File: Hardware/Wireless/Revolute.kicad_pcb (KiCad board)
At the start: 4 copper layers, 20 x 20 mm, 54 parts, among them Q1 AO3407, U1 BQ27441-G1, U2 nrf52833_qfn40, U3 AS5600, U4 AP2112K-3.3, U5 BQ24075RGT, U7 MAX16054, X1 32.768 kHz, X2 32MHZ

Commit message: worked on wireless
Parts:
- removed the ? at (171.0, 95.0)
- removed Q1: AO3407, Package_TO_SOT_SMD:SOT-23
- removed R10: 5.1K, Resistor_SMD:R_0402_1005Metric
- removed U7: MAX16054, Package_TO_SOT_SMD:SOT-23-6
- added ?: , , F.Cu at (179.1, 96.5)
- added ?: , , F.Cu at (178.7, 94.7)
- added U6: Button, Library:buttoncompliant, F.Cu at (171.0, 95.0)
- added U8: ~, Library:BK13C06-10DP, B.Cu at (175.0, 94.8)
- AE1: value ANT3216LL00R2400A -> Antenna
- moved C26 4.76 mm to (175.6, 102.8)
- moved C22 4.76 mm to (175.6, 101.8)
- moved U4 1.37 mm to (176.4, 99.1), turned to 90 degrees
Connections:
- C22 pad 1: vSYSTEM -> OUT
- C26 pad 1: vSYSTEM -> OUT
- U2 pad 33: unconnected-(U2-P0.28/AIN4-Pad33) -> Net-(U2-P0.28/AIN4)
- U4 pad 1: vSYSTEM -> OUT
- U4 pad 3: vSYSTEM -> OUT
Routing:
- net D+: track 0.76 -> 19.8 mm, vias 1 -> 2
- net D-: track 0.50 -> 17.6 mm, vias 1 -> 2
- net swd: track 0.74 -> 13.4 mm, vias 1 -> 2
- net swc: track 0.48 -> 13.0 mm, vias 1 -> 2
- net RESET: track 0.80 -> 13.1 mm, vias 1 -> 2
- net Net-(U7-IN): track 9.19 -> 0.00 mm, vias 1 -> 0
- net GND: track 20.3 -> 27.7 mm, vias 10 -> 24
- net vSYSTEM: track 7.14 -> 0.00 mm
- net OUT: track 22.9 -> 17.7 mm
- net Net-(Q1-G): track 4.33 -> 0.00 mm
- net Batteryin: track 6.56 -> 10.3 mm, vias 2 -> 4
- net VDD_nRF: track 18.6 -> 22.3 mm, vias 8 -> 10
- net Net-(U2-P0.28/AIN4): track 0.00 -> 3.53 mm, vias 0 -> 1
- net CLEAR: track 2.53 -> 0.00 mm
- net P0.15: track 28.6 -> 31.0 mm, vias 3 -> 4
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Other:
- board size 20 x 20 mm -> 19.8 x 20 mm
- board text added: "D+"
- board text added: "D-"
- board text added: "GND"
- board text added: "RST"
- board text added: "SWC"
- board text added: "SWD"
- board text added: "VDD"

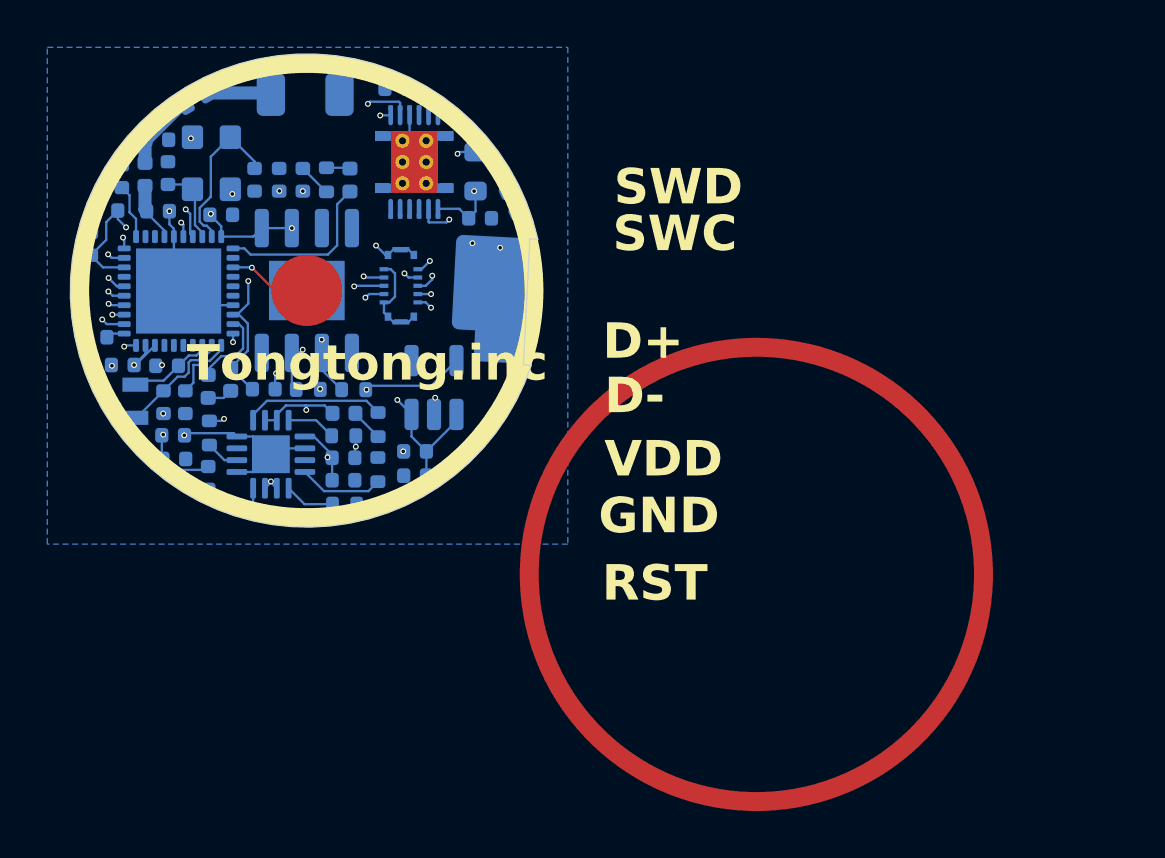
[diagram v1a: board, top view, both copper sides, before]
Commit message: added debug board (work in progress)
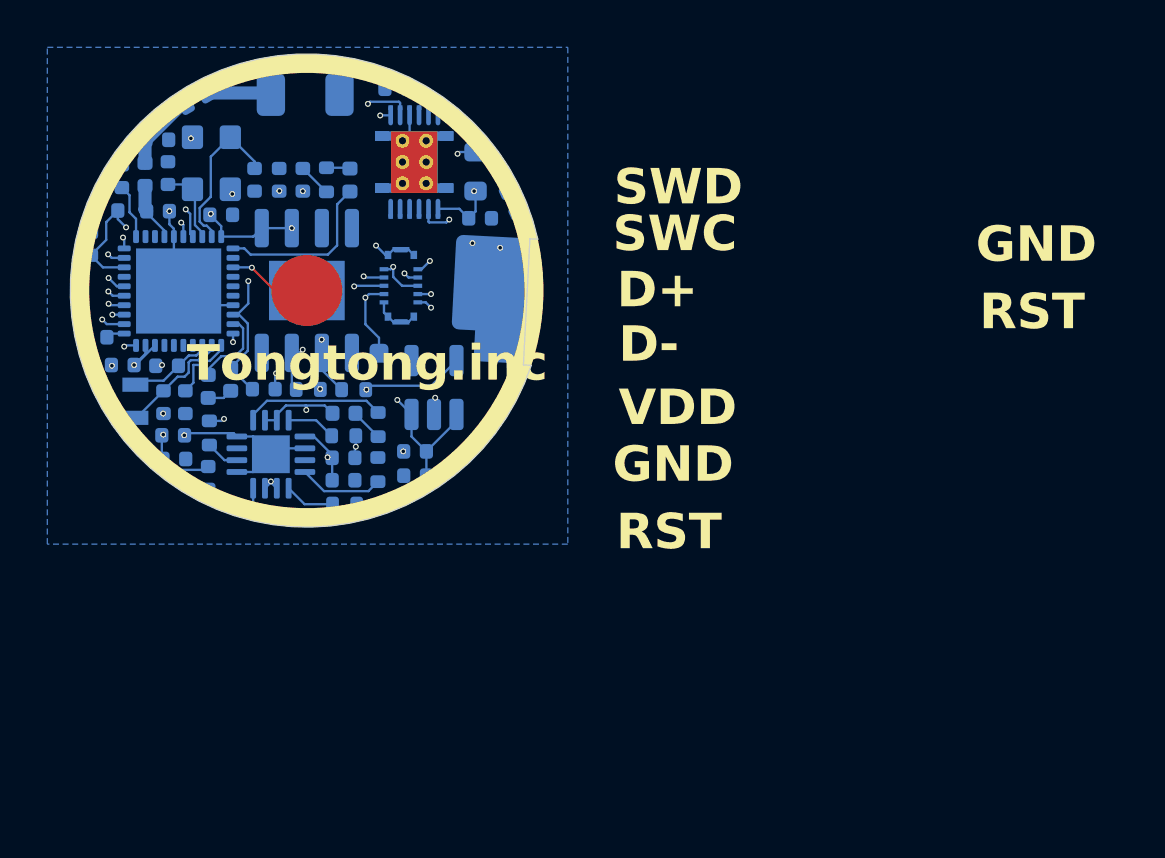
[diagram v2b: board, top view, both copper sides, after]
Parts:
- added ?: , , F.Cu at (174.1, 97.7)
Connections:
- U8 pad 1: GND -> OUT
- U8 pad 8: VDD_nRF -> OUT
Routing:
- net OUT: track 17.7 -> 25.4 mm, vias 3 -> 4
- net RESET: track 13.1 -> 15.7 mm
- net GND: track 27.7 -> 25.6 mm
- net VDD_nRF: track 22.3 -> 21.4 mm, vias 10 -> 9
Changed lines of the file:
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@@
   (net 59 "GPOUT")
   (footprint "" (layer "F.Cu")
+    (at 174.05 97.65)
+    (fp_text reference "" (at 0 0) (layer "F.SilkS")
+        (effects (font (size 1.27 1.27) (thickness 0.15)))
+    )
+    (fp_text value "" (at 0 0) (layer "F.SilkS")
+        (effects (font (size 1.27 1.27) (thickness 0.15)))
+    )
+    (pad "4" smd roundrect (at 0 0 90) (size 0.8 0.8) (layers "B.Cu" "B.Paste" "B.Mask") (roundrect_rratio 0.25)
+      (net 19 "RESET") (pinfunction "NC") (pintype "no_connect"))
+  )
+  (footprint "" (layer "F.Cu")
     (at 179.121196 96.534972 -3)
     (fp_text reference "" (at 0 0 177) (layer "F.SilkS")
@@
       (stroke (width 0.15) (type default)) (fill none) (layer "B.SilkS"))
     (pad "1" smd rect (at -0.7 0.715 270) (size 0.18 0.37) (layers "B.Cu" "B.Paste" "B.Mask")
-      (net 1 "GND") (pinfunction "VDD") (pintype "bidirectional") (thermal_bridge_angle 45))
+      (net 9 "OUT") (pinfunction "VDD") (pintype "bidirectional") (thermal_bridge_angle 45))
     (pad "2" smd rect (at -0.35 0.715 270) (size 0.18 0.37) (layers "B.Cu" "B.Paste" "B.Mask")
       (net 6 "swc") (pinfunction "PDM_DAT") (pintype "bidirectional") (thermal_bridge_angle 45))
@@
       (net 16 "P0.17") (pinfunction "B2") (pintype "bidirectional") (thermal_bridge_angle 45))
     (pad "8" smd rect (at 0 -0.715 270) (size 0.18 0.37) (layers "B.Cu" "B.Paste" "B.Mask")
-      (net 2 "VDD_nRF") (pinfunction "APDS_IRQ") (pintype "bidirectional") (thermal_bridge_angle 45))
+      (net 9 "OUT") (pinfunction "APDS_IRQ") (pintype "bidirectional") (thermal_bridge_angle 45))
     (pad "9" smd rect (at 0.35 -0.715 270) (size 0.18 0.37) (layers "B.Cu" "B.Paste" "B.Mask")
       (net 57 "D+") (pinfunction "NFC1") (pintype "bidirectional") (thermal_bridge_angle 45))
@@
     )
   )
-  (gr_circle (center 190 107) (end 199.6 107)
+  (gr_circle (center 171 95) (end 180.6 95)
     (stroke (width 0.8) (type default)) (fill none) (layer "F.Cu"))
   (gr_circle (center 171 95) (end 180.6 95)
@@
   (gr_circle (center 180.171281 92.191197) (end 181.171281 92.191197)
     (stroke (width 0.01) (type default)) (fill none) (layer "User.1"))
-  (gr_text "VDD" (at 183.575 103) (layer "F.SilkS")
+  (gr_text "GND" (at 199.275 93.925) (layer "F.SilkS")
+    (effects (font (size 1.5 1.5) (thickness 0.3) bold) (justify left bottom))
+  )
+  (gr_text "VDD" (at 184.175 100.825) (layer "F.SilkS")
     (effects (font (size 1.5 1.5) (thickness 0.3) bold) (justify left bottom))
   )
@@
     (effects (font (size 1.5 1.5) (thickness 0.3) bold) (justify left bottom))
   )
-  (gr_text "D-" (at 183.575 100.325) (layer "F.SilkS")
+  (gr_text "RST" (at 199.425 96.775) (layer "F.SilkS")
+    (effects (font (size 1.5 1.5) (thickness 0.3) bold) (justify left bottom))
+  )
+  (gr_text "D-" (at 184.175 98.15) (layer "F.SilkS")
     (effects (font (size 1.5 1.5) (thickness 0.3) bold) (justify left bottom))
   )
-  (gr_text "D+" (at 183.5 98.025) (layer "F.SilkS")
+  (gr_text "D+" (at 184.1 95.85) (layer "F.SilkS")
     (effects (font (size 1.5 1.5) (thickness 0.3) bold) (justify left bottom))
   )
-  (gr_text "RST" (at 183.475 108.25) (layer "F.SilkS")
+  (gr_text "RST" (at 184.075 106.075) (layer "F.SilkS")
     (effects (font (size 1.5 1.5) (thickness 0.3) bold) (justify left bottom))
   )
-  (gr_text "GND" (at 183.325 105.4) (layer "F.SilkS")
+  (gr_text "GND" (at 183.925 103.225) (layer "F.SilkS")
     (effects (font (size 1.5 1.5) (thickness 0.3) bold) (justify left bottom))
   )
@@
   (segment (start 174.3 86.26) (end 174.1 86.06) (width 0.1) (layer "B.Cu") (net 1))
   (segment (start 166.164828 88.52) (end 166.15 88.52) (width 0.1) (layer "B.Cu") (net 1))
-  (segment (start 174.545 94.1) (end 174.725 94.28) (width 0.1) (layer "B.Cu") (net 1))
   (segment (start 173.105453 104.031759) (end 173.761283 104.031759) (width 0.1) (layer "B.Cu") (net 1))
   (segment (start 175.092732 101.8) (end 175.075 101.8) (width 0.1) (layer "B.Cu") (net 1))
@@
   (segment (start 165.92 101.03) (end 167.9025 101.03) (width 0.1) (layer "B.Cu") (net 1))
   (segment (start 167.764828 90.72) (end 167.764828 90.834828) (width 0.1) (layer "B.Cu") (net 1))
-  (segment (start 174.725 94.28) (end 174.725 95.26) (width 0.1) (layer "B.Cu") (net 1))
   (segment (start 174.26 95.935) (end 174.26 95.5) (width 0.1) (layer "B.Cu") (net 1))
   (segment (start 169.66 99.17) (end 169.66 98.54) (width 0.1) (layer "B.Cu") (net 1))
-  (segment (start 174.26 94.1) (end 174.545 94.1) (width 0.1) (layer "B.Cu") (net 1))
   (segment (start 162.738572 98.148521) (end 162.738572 98.158572) (width 0.1) (layer "B.Cu") (net 1))
-  (segment (start 174.485 95.5) (end 174.26 95.5) (width 0.1) (layer "B.Cu") (net 1))
   (segment (start 173.105453 104.031759) (end 172.620451 104.516761) (width 0.1) (layer "B.Cu") (net 1))
-  (segment (start 174.725 95.26) (end 174.485 95.5) (width 0.1) (layer "B.Cu") (net 1))
   (segment (start 164.614341 98.181217) (end 164.848783 98.181217) (width 0.1) (layer "B.Cu") (net 1))
   (segment (start 165.38 94.82) (end 165.58 95.02) (width 0.1) (layer "B.Cu") (net 1))
@@
   (via (at 163.698572 98.148521) (size 0.25) (drill 0.15) (layers "F.Cu" "B.Cu") (net 2))
   (via (at 163.36 92.33) (size 0.25) (drill 0.15) (layers "F.Cu" "B.Cu") (net 2))
-  (via (at 176.3 94.375) (size 0.25) (drill 0.15) (layers "F.Cu" "B.Cu") (net 2))
   (via (at 170.365 92.3625) (size 0.25) (drill 0.15) (layers "F.Cu" "B.Cu") (net 2))
   (via (at 166.94 91.76) (size 0.25) (drill 0.15) (layers "F.Cu" "B.Cu") (net 2))
@@
   (segment (start 175.52 93.495) (end 175.3 93.275) (width 0.1) (layer "B.Cu") (net 2))
   (segment (start 171.57 99.17) (end 171.56 99.16) (width 0.1) (layer "B.Cu") (net 2))
-  (segment (start 176.025 94.8) (end 176.3 94.525) (width 0.1) (layer "B.Cu") (net 2))
   (segment (start 173.49 99.19) (end 173.52 99.19) (width 0.1) (layer "B.Cu") (net 2))
   (segment (start 164.18 97.32) (end 164.18 97.667093) (width 0.1) (layer "B.Cu") (net 2))
@@
   (segment (start 164.87 101.12) (end 164.9 101.12) (width 0.1) (layer "B.Cu") (net 2))
   (segment (start 161.87 93.51) (end 161.85 93.51) (width 0.1) (layer "B.Cu") (net 2))
-  (segment (start 175.69 94.8) (end 176.025 94.8) (width 0.1) (layer "B.Cu") (net 2))
   (segment (start 168.7375 92.72) (end 169.095 92.3625) (width 0.1) (layer "B.Cu") (net 2))
   (segment (start 167.38 92.278932) (end 166.900078 91.79901) (width 0.1) (layer "B.Cu") (net 2))
@@
   (segment (start 167.88 96.82) (end 167.88 97.18) (width 0.1) (layer "B.Cu") (net 2))
   (segment (start 174.975 93.275) (end 174.65 93.275) (width 0.1) (layer "B.Cu") (net 2))
-  (segment (start 176.3 94.525) (end 176.3 94.375) (width 0.1) (layer "B.Cu") (net 2))
   (segment (start 174.65 93.275) (end 174.43 93.495) (width 0.1) (layer "B.Cu") (net 2))
   (segment (start 162.52 92.86) (end 162.52 92.11) (width 0.1) (layer "B.Cu") (net 2))
@@
   (via (at 170.975 100.05) (size 0.25) (drill 0.15) (layers "F.Cu" "B.Cu") (net 9))
   (via (at 174.825 99.625) (size 0.25) (drill 0.15) (layers "F.Cu" "B.Cu") (net 9))
+  (via (at 174.65 94) (size 0.25) (drill 0.15) (layers "F.Cu" "B.Cu") (net 9))
   (via (at 167.5 100.425) (size 0.25) (drill 0.15) (layers "F.Cu" "B.Cu") (net 9))
   (segment (start 170.6 100.425) (end 170.975 100.05) (width 0.1) (layer "In2.Cu") (net 9))
   (segment (start 167.5 100.425) (end 170.6 100.425) (width 0.1) (layer "In2.Cu") (net 9))
+  (segment (start 174.65 99.45) (end 174.825 99.625) (width 0.1) (layer "In2.Cu") (net 9))
+  (segment (start 174.65 94) (end 174.65 99.45) (width 0.1) (layer "In2.Cu") (net 9))
   (segment (start 174.4 100.05) (end 174.825 99.625) (width 0.1) (layer "In2.Cu") (net 9))
   (segment (start 170.975 100.05) (end 174.4 100.05) (width 0.1) (layer "In2.Cu") (net 9))
@@
   (segment (start 171.755 99.86) (end 172.085 100.19) (width 0.1) (layer "B.Cu") (net 9))
   (segment (start 170.975 100.05) (end 170.975 99.885) (width 0.1) (layer "B.Cu") (net 9))
+  (segment (start 174.65 94.425) (end 175.025 94.8) (width 0.1) (layer "B.Cu") (net 9))
   (segment (start 176.052732 101.8) (end 176.052732 102.822732) (width 0.1) (layer "B.Cu") (net 9))
   (segment (start 169.73 100.24448) (end 170.11448 99.86) (width 0.1) (layer "B.Cu") (net 9))
   (segment (start 176.052732 102.822732) (end 176.055 102.825) (width 0.1) (layer "B.Cu") (net 9))
+  (segment (start 174.26 94.1) (end 174.55 94.1) (width 0.1) (layer "B.Cu") (net 9))
+  (segment (start 174.55 94.1) (end 174.65 94) (width 0.1) (layer "B.Cu") (net 9))
   (segment (start 170.975 99.885) (end 170.95 99.86) (width 0.1) (layer "B.Cu") (net 9))
+  (segment (start 174.65 94) (end 174.65 94.425) (width 0.1) (layer "B.Cu") (net 9))
   (segment (start 177.325 100.2375) (end 177.325 100.527732) (width 0.1) (layer "B.Cu") (net 9))
   (segment (start 175.425 100.225) (end 174.825 99.625) (width 0.1) (layer "B.Cu") (net 9))
+  (segment (start 175.025 94.8) (end 175.69 94.8) (width 0.1) (layer "B.Cu") (net 9))
   (segment (start 169.73 100.4825) (end 169.73 100.24448) (width 0.1) (layer "B.Cu") (net 9))
   (segment (start 169.23 100.4825) (end 169.73 100.4825) (width 0.1) (layer "B.Cu") (net 9))
@@
   (segment (start 173.15 95.625) (end 164.6 95.625) (width 0.1) (layer "In1.Cu") (net 19))
   (segment (start 173.475 95.3) (end 173.625 95.15) (width 0.1) (layer "B.Cu") (net 19))
+  (segment (start 173.475 96.425) (end 174.05 97) (width 0.1) (layer "B.Cu") (net 19))
   (segment (start 162.97 94.82) (end 162.62 94.47) (width 0.1) (layer "B.Cu") (net 19))
   (segment (start 163.28 94.82) (end 162.97 94.82) (width 0.1) (layer "B.Cu") (net 19))
+  (segment (start 174.05 97) (end 174.05 97.65) (width 0.1) (layer "B.Cu") (net 19))
+  (segment (start 173.475 95.3) (end 173.475 96.425) (width 0.1) (layer "B.Cu") (net 19))
   (segment (start 173.625 95.15) (end 174.26 95.15) (width 0.1) (layer "B.Cu") (net 19))
   (segment (start 166.701339 97.774181) (end 166.98 97.49552) (width 0.1) (layer "B.Cu") (net 21))

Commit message: update ibom
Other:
- board text removed: "D+"
- board text removed: "D-"
- board text removed: "SWC"
- board text removed: "SWD"
- board text removed: "VDD"
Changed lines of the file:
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@@
-    (effects (font (size 1.5 1.5) (thickness 0.3) bold) (justify left bottom))
-  )
-  (gr_text "VDD" (at 184.175 100.825) (layer "F.SilkS")
-    (effects (font (size 1.5 1.5) (thickness 0.3) bold) (justify left bottom))
-  )
-  (gr_text "SWC" (at 183.925 93.475) (layer "F.SilkS")
     (effects (font (size 1.5 1.5) (thickness 0.3) bold) (justify left bottom))
   )
@@
     (effects (font (size 1.5 1.5) (thickness 0.3) bold) (justify left bottom))
   )
-  (gr_text "D-" (at 184.175 98.15) (layer "F.SilkS")
-    (effects (font (size 1.5 1.5) (thickness 0.3) bold) (justify left bottom))
-  )
-  (gr_text "D+" (at 184.1 95.85) (layer "F.SilkS")
-    (effects (font (size 1.5 1.5) (thickness 0.3) bold) (justify left bottom))
-  )
-  (gr_text "RST" (at 184.075 106.075) (layer "F.SilkS")
-    (effects (font (size 1.5 1.5) (thickness 0.3) bold) (justify left bottom))
-  )
-  (gr_text "GND" (at 183.925 103.225) (layer "F.SilkS")
-    (effects (font (size 1.5 1.5) (thickness 0.3) bold) (justify left bottom))
-  )
-  (gr_text "SWD" (at 183.975 91.5) (layer "F.SilkS")
-    (effects (font (size 1.5 1.5) (thickness 0.3) bold) (justify left bottom))
-  )

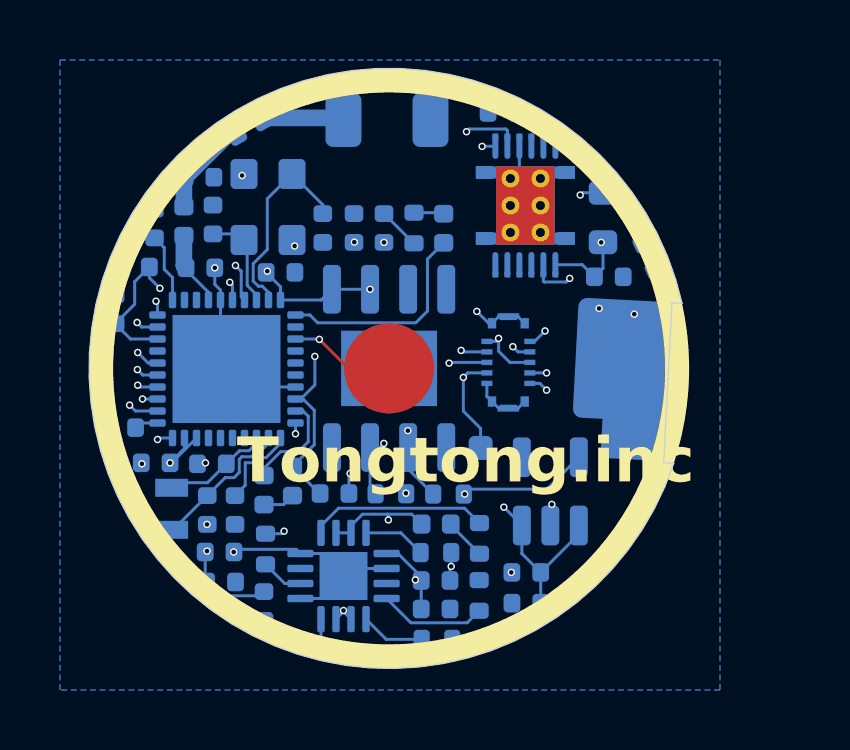
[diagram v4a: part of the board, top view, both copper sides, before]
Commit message: changed via hole sizes
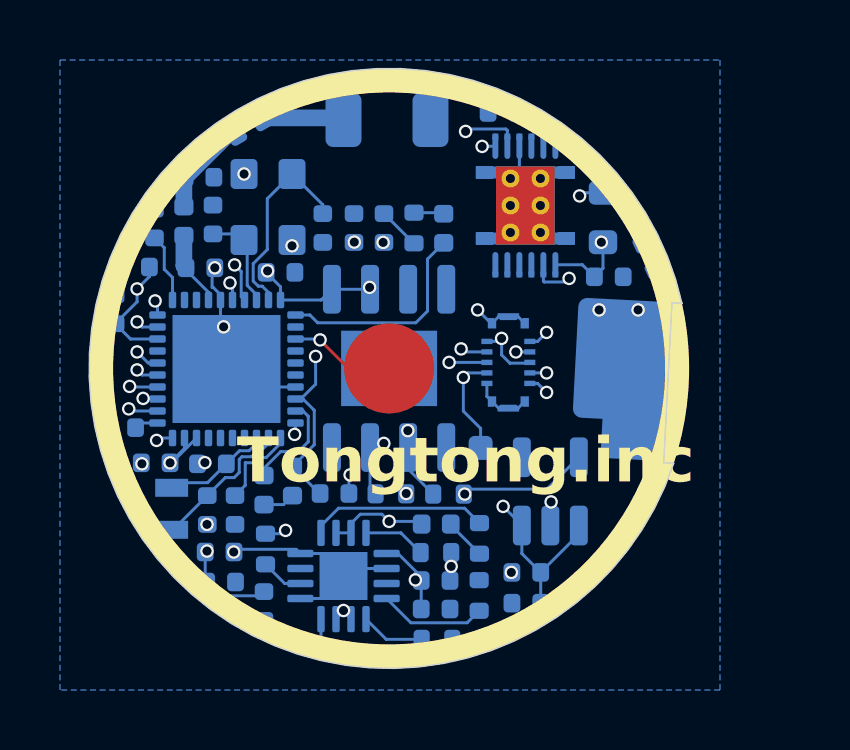
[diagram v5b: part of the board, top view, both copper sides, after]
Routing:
- net GND: track 25.6 -> 27.5 mm, vias 24 -> 25
- net Batteryin: track 10.3 -> 12.2 mm
- net VDD_nRF: track 21.4 -> 20.6 mm
- net P0.15: track 31.0 -> 31.5 mm

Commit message: fixed design
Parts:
- added ?: , , F.Cu at (191.3, 94.8)
- added REF**: Pogofemale, Library:Pogofemale, F.Cu at (191.5, 97.8)
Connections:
- U8 pad 1: OUT -> VBUS
- U8 pad 8: OUT -> VBUS
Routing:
- net VBUS: track 13.9 -> 27.7 mm, vias 2 -> 3
- net OUT: track 25.5 -> 17.6 mm, vias 4 -> 3
- net GND: track 27.5 -> 29.8 mm, vias 25 -> 26
- net D-: track 17.6 -> 16.8 mm
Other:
- board text removed: "GND"
- board text removed: "RST"
